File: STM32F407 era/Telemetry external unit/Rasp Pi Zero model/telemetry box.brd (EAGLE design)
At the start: 160 x 100 mm, 14 parts, among them U1 SC18IM700IPW,112

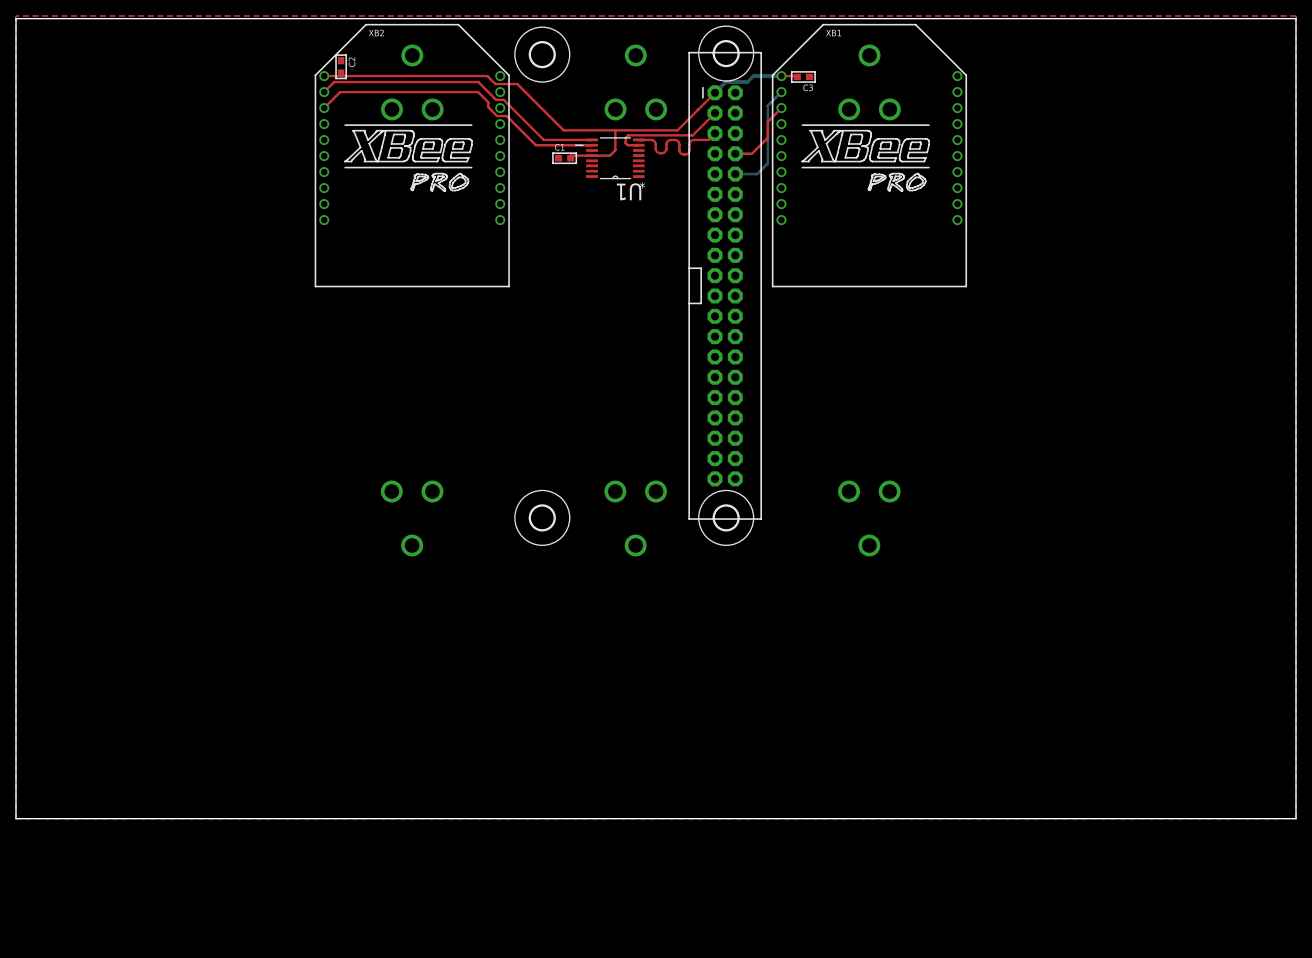
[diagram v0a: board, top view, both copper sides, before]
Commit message: started reworking the board for better charging
started reworking the battery solution to incorporate parallel cell
charging.
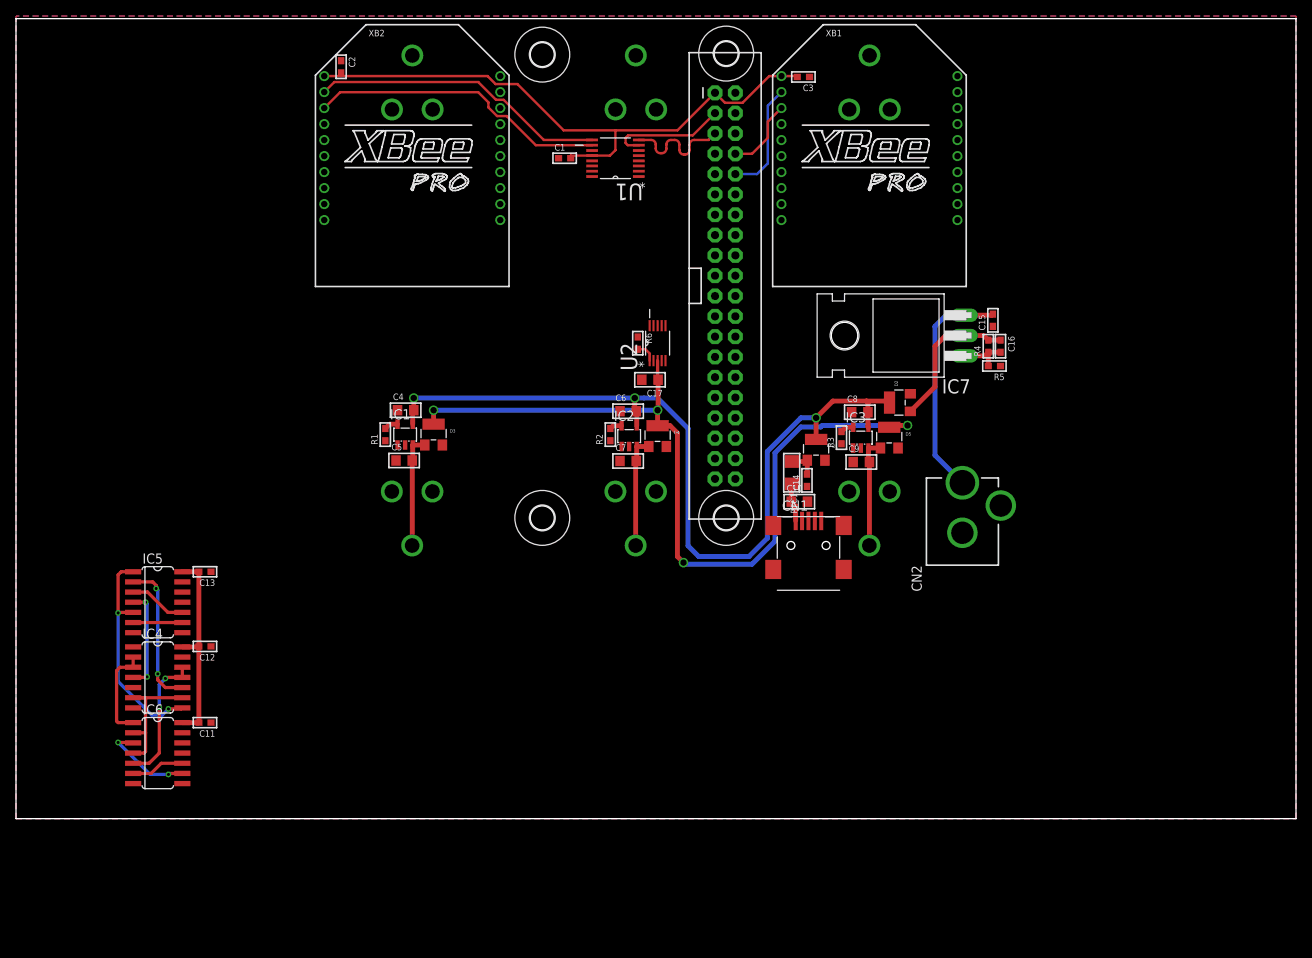
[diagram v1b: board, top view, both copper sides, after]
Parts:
- added C10, C17, C4, C5, C6, C7, C8, C9: 10u, microbuilder:_0805
- added C11, C12, C13, C14, C15: 100n, microbuilder:_0603
- added C16: 1u-T, microbuilder:_0603
- added CN1: (no value), adafruit:USB-MINIB
- added CN2: (no value), adafruit:DCJACK_2MM_PTH
- added D1, D2, D3, D4, D5: (no value), adafruit:SOT23-W
- added IC1, IC2, IC3: MCP73831/OT, adafruit:SOT23-5L
- added IC4: 74AC14D, 74xx-eu:SO14
- added IC5: 74HC08D, 74xx-eu:SO14
- added IC6: 74AC32D, 74xx-eu:SO14
- added IC7: 317T, linear:TO220H
- added PTC1: (no value), microbuilder:1206
- added R1, R2, R3: 5k, microbuilder:_0603
- added R4: 240, microbuilder:_0603
- added R5: 732, microbuilder:_0603
- added R6: 30k1, microbuilder:_0603
- added U2: LTC3402EMSPBF, LTC_By_element14_Batch_1:SOP50P490X110-10N
- turned BAT1 to 90 degrees
- turned BAT2 to 90 degrees
- turned BAT3 to 90 degrees
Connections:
- removed net +: BAT1.PWR@1, BAT2.PWR@1, BAT3.PWR@1
- removed net -: BAT1.GND@1, BAT2.GND@1, BAT3.GND@1
- new net BAT-STAT1: IC1.1, IC4.1
- new net BAT-STAT2: IC2.1, IC4.5
- new net BAT-STAT3: IC3.1, IC4.13
- new net N$1: BAT2.PWR@1, C7.2, D4.1, IC2.3
- new net N$10: IC4.6, IC4.9, IC6.2, IC6.4
- new net N$11: IC4.2, IC4.3, IC6.1
- new net N$12: IC5.6, IC5.9
- new net N$13: IC4.11, IC4.12, IC6.5
- new net N$14: IC4.8, IC5.1, IC5.5
- new net N$15: IC4.10, IC5.2
- new net N$16: IC4.4, IC5.4
- new net N$17: C10.1, CN1.VBUS, PTC1.2
- new net N$18: C16.2, IC7.1, R4.1, R5.2
- new net N$19: R6.2, U2.1
- new net N$2: IC1.5, R1.2
- new net N$20: C16.1, D2.1, IC7.2, R4.2
- new net N$21: C14.2, D1.1, PTC1.1
- new net N$22: C15.2, CN2.PWR, IC7.3
- new net N$3: IC2.5, R2.2
- new net N$4: BAT1.PWR@1, C5.2, D3.1, IC1.3
- new net N$5: IC5.10, IC5.3
- new net N$6: IC6.10, IC6.6
- new net N$7: IC3.5, R3.2
- new net N$8: BAT3.PWR@1, C9.2, D5.1, IC3.3
- new net N$9: IC6.3, IC6.9
- new net VBAT: C17.1, D3.3, D4.3, D5.3, U2.3
- new net VCC: C4.2, C6.2, C8.2, D1.3, D2.3, IC1.4, IC2.4, IC3.4
- net 5.0V: now also C11.2, C12.2, C13.2, IC4.14, IC5.14, IC6.14
- net GND: now also BAT1.GND@1, BAT2.GND@1, BAT3.GND@1, C10.2, C11.1, C12.1, C13.1, C14.1, C15.1, C17.2, C4.1, C5.1, C6.1, C7.1, C8.1, C9.1, CN1.GND, CN2.GND, CN2.GNDBREAK, IC1.2, IC2.2, IC3.2, IC4.7, IC5.12, IC5.13, IC5.7, IC6.12, IC6.13, IC6.7, R1.1, R2.1, R3.1, R5.1, R6.1, U2.2, U2.5
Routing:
- net VCC: track 0.00 -> 103.7 mm, vias 0 -> 3
- net VBAT: track 0.00 -> 101.4 mm, vias 0 -> 4
- net N$22: track 0.00 -> 28.8 mm
- net N$14: track 0.00 -> 27.4 mm, vias 0 -> 2
- net 5.0V: track 0.00 -> 25.1 mm
- net N$15: track 0.00 -> 18.4 mm, vias 0 -> 2
- net N$20: track 0.00 -> 18.4 mm
- net N$10: track 0.00 -> 17.6 mm
- net N$13: track 0.00 -> 16.9 mm, vias 0 -> 2
- net N$4: track 0.00 -> 14.1 mm
- net N$1: track 0.00 -> 13.9 mm
- net N$8: track 0.00 -> 13.7 mm
- net N$16: track 0.00 -> 12.7 mm, vias 0 -> 2
- net N$11: track 0.00 -> 12.0 mm
- net N$9: track 0.00 -> 11.6 mm, vias 0 -> 2
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
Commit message: minor changes to layout
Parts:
- added C18, C19: 1u, microbuilder:_0603
- added R7, R8: 850, microbuilder:_0603
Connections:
- new net LAPRSSISENSE: C19.2, R8.2
- new net N$23: R7.1, XB1.6
- new net N$24: R8.1, XB2.6
- new net TELERSSISENSE: C18.2, R7.2
- net 3.3V: now also XB1.5, XB2.5
- net GND: now also C18.1, C19.1
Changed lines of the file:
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@@
 <element name="C17" library="microbuilder" package="_0805" value="10u" x="79.248" y="54.864" rot="R180"/>
 <element name="R6" library="microbuilder" package="_0603" value="30k1" x="77.724" y="59.436" rot="R270"/>
+<element name="R7" library="microbuilder" package="_0603" value="850" x="1.6891" y="-2.26695"/>
+<element name="C18" library="microbuilder" package="_0603" value="1u" x="1.6891" y="-6.4008"/>
+<element name="R8" library="microbuilder" package="_0603" value="850" x="1.6891" y="-10.53465"/>
+<element name="C19" library="microbuilder" package="_0603" value="1u" x="1.6891" y="-14.6685"/>
 </elements>
 <signals>
@@
 <wire x1="72.009" y1="82.8802" x2="69.342" y2="82.8802" width="0.3048" layer="1"/>
 <wire x1="69.342" y1="82.8802" x2="69.342" y2="82.55" width="0.3048" layer="1"/>
-<wire x1="62.6745" y1="91.821" x2="68.453" y2="86.0425" width="0.3048" layer="1"/>
+<wire x1="61.29655" y1="91.821" x2="67.07505" y2="86.0425" width="0.3048" layer="1"/>
 <wire x1="72.009" y1="82.8802" x2="74.2442" y2="82.8802" width="0.3048" layer="1"/>
 <wire x1="74.2442" y1="82.8802" x2="74.93" y2="83.566" width="0.3048" layer="1"/>
 <wire x1="74.93" y1="83.566" x2="74.93" y2="86.0425" width="0.3048" layer="1"/>
-<wire x1="62.6745" y1="91.821" x2="59.944" y2="91.821" width="0.3048" layer="1"/>
+<wire x1="61.29655" y1="91.821" x2="59.944" y2="91.821" width="0.3048" layer="1"/>
 <wire x1="59.944" y1="91.821" x2="58.945" y2="92.82" width="0.3048" layer="1"/>
 <wire x1="58.945" y1="92.82" x2="40.64" y2="92.82" width="0.3048" layer="1"/>
 <wire x1="40.64" y1="92.82" x2="38.53" y2="92.82" width="0.3048" layer="1"/>
 <wire x1="40.64" y1="93.218" x2="40.64" y2="92.82" width="0.3048" layer="1"/>
-<wire x1="68.453" y1="86.0425" x2="74.93" y2="86.0425" width="0.3048" layer="1"/>
+<wire x1="67.07505" y1="86.0425" x2="74.93" y2="86.0425" width="0.3048" layer="1"/>
 <wire x1="74.93" y1="86.0425" x2="82.6897" y2="86.0425" width="0.3048" layer="1"/>
 <wire x1="82.6897" y1="86.0425" x2="87.376" y2="90.7288" width="0.3048" layer="1"/>
@@
 <wire x1="90.81135" y1="89.47785" x2="94.1535" y2="92.82" width="0.3048" layer="1"/>
 <wire x1="94.1535" y1="92.82" x2="95.68" y2="92.82" width="0.3048" layer="1"/>
-<wire x1="82.6897" y1="86.0425" x2="87.376" y2="70.4088" width="0" layer="19" extent="1-1"/>
+<contactref element="XB1" pad="5"/>
+<contactref element="XB2" pad="5"/>
+<wire x1="90.81135" y1="89.47785" x2="95.68" y2="84.82" width="0" layer="19" extent="1-1"/>
+<wire x1="38.53" y1="84.82" x2="38.53" y2="92.82" width="0" layer="19" extent="1-1"/>
+<wire x1="87.376" y1="70.4088" x2="82.6897" y2="86.0425" width="0" layer="19" extent="1-1"/>
 </signal>
 <signal name="GND">
@@
 <contactref element="U2" pad="2"/>
 <contactref element="R6" pad="1"/>
+<contactref element="C18" pad="1"/>
+<contactref element="C19" pad="1"/>
+<wire x1="0.9271" y1="-6.4008" x2="0.9271" y2="-14.6685" width="0" layer="19" extent="1-1"/>
+<wire x1="14.6431" y1="4.3815" x2="0.9271" y2="-6.4008" width="0" layer="19" extent="1-1"/>
 </signal>
 <signal name="5.0V">
@@
 <wire x1="78.6765" y1="58.674" x2="77.724" y2="58.674" width="0.3048" layer="1"/>
 </signal>
+<signal name="N$23">
+<contactref element="XB1" pad="6"/>
+<contactref element="R7" pad="1"/>
+<wire x1="0.9271" y1="-2.26695" x2="95.68" y2="82.82" width="0" layer="19" extent="1-1"/>
+</signal>
+<signal name="TELERSSISENSE">
+<contactref element="R7" pad="2"/>
+<contactref element="C18" pad="2"/>
+<wire x1="2.4511" y1="-2.26695" x2="2.4511" y2="-6.4008" width="0" layer="19" extent="1-1"/>
+</signal>
+<signal name="N$24">
+<contactref element="XB2" pad="6"/>
+<contactref element="R8" pad="1"/>
+<wire x1="0.9271" y1="-10.53465" x2="38.53" y2="82.82" width="0" layer="19" extent="1-1"/>
+</signal>
+<signal name="LAPRSSISENSE">
+<contactref element="R8" pad="2"/>
+<contactref element="C19" pad="2"/>
+<wire x1="2.4511" y1="-10.53465" x2="2.4511" y2="-14.6685" width="0" layer="19" extent="1-1"/>
+</signal>
 </signals>

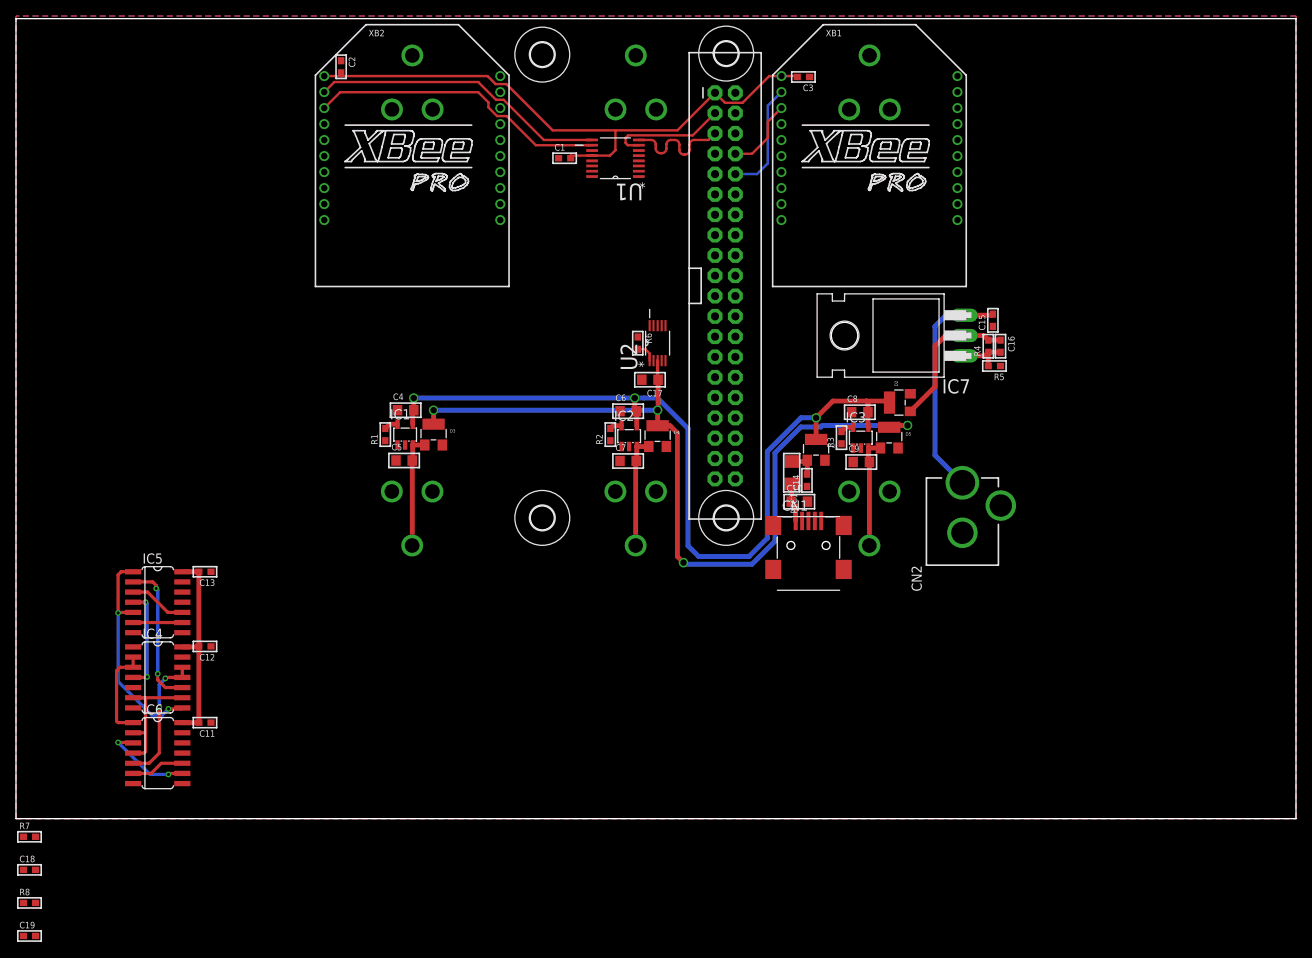
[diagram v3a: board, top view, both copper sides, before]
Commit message: started working on the power circuitry
started work on 5V boost circuit for the battery powered operation
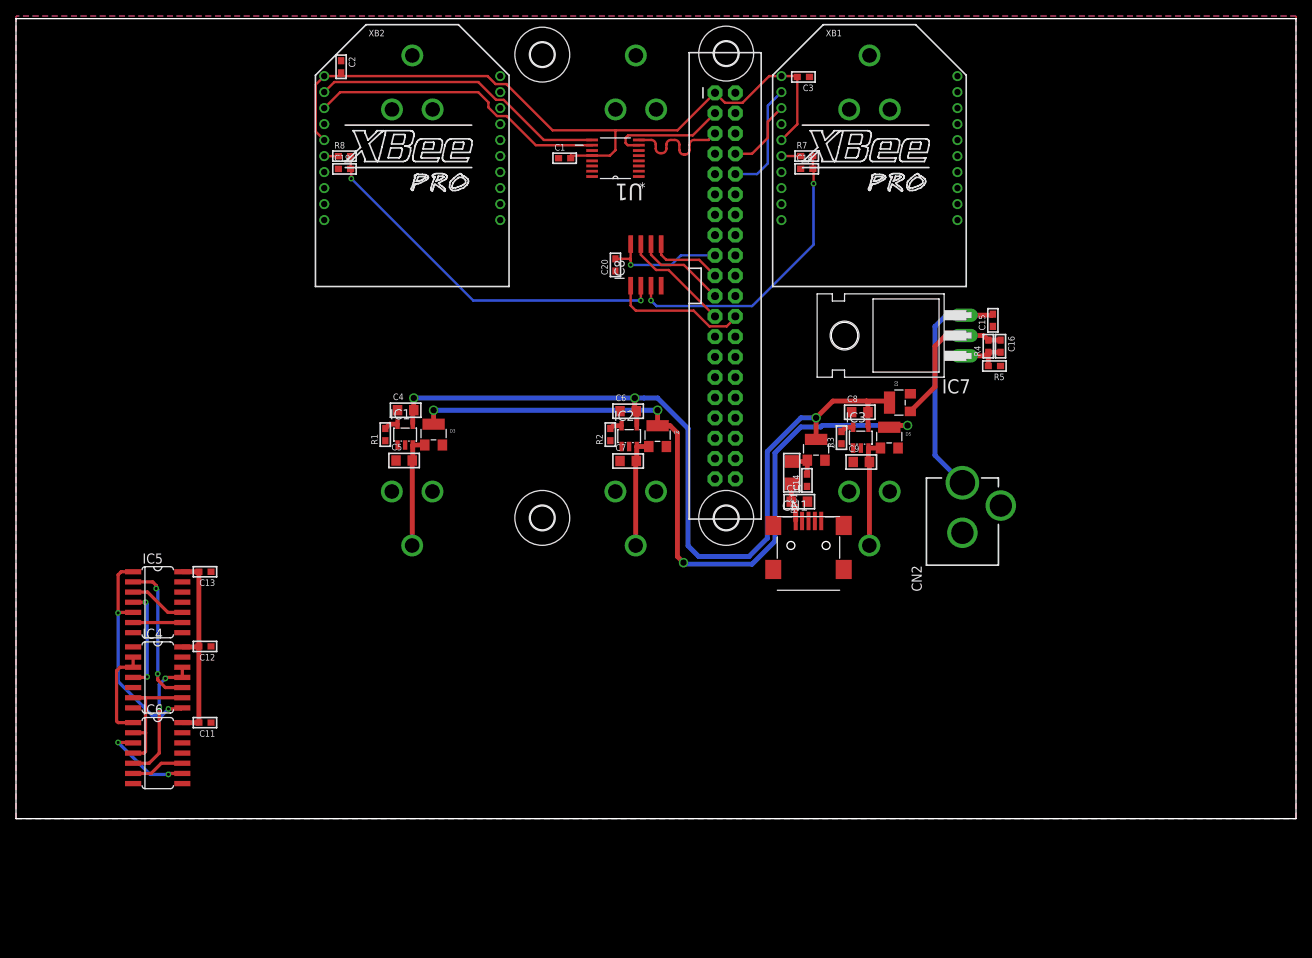
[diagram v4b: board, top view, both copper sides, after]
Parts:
- removed C17: 10u, microbuilder:_0805
- removed R6: 30k1, microbuilder:_0603
- removed U2: LTC3402EMSPBF, LTC_By_element14_Batch_1:SOP50P490X110-10N
- added C20: 100n, microbuilder:_0603
- added IC8: MCP3202SN, microchip:SO-08
- moved C18 130.8 mm to (98.8, 81.2)
- moved R7 129.1 mm to (98.8, 82.8)
- moved C19 103.7 mm to (41.1, 81.2)
- moved R8 101.3 mm to (41.1, 82.8)
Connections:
- removed net N$19: R6.2, U2.1
- new net CE0: IC8.1, JP1.24
- new net MISO: IC8.6, JP1.21
- new net MOSI: IC8.5, JP1.19
- new net SCLK: IC8.7, JP1.23
- net 3.3V: now also C11.2, C12.2, C13.2, C20.2, IC4.14, IC5.14, IC6.14, IC8.8
- net 5.0V: no longer C11.2, C12.2, C13.2, IC4.14, IC5.14, IC6.14
- net GND: now also C20.1, IC8.4; no longer C17.2, R6.1, U2.2, U2.5
- net LAPRSSISENSE: now also IC8.2
- net TELERSSISENSE: now also IC8.3
- net VBAT: no longer C17.1, U2.3
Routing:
- net 3.3V: track 74.9 -> 133.2 mm, vias 0 -> 1
- net LAPRSSISENSE: track 0.00 -> 47.2 mm, vias 0 -> 2
- net TELERSSISENSE: track 0.00 -> 36.8 mm, vias 0 -> 2
- net 5.0V: track 25.1 -> 0.00 mm
- net CE0: track 0.00 -> 17.3 mm
- net SCLK: track 0.00 -> 13.8 mm
- net MISO: track 0.00 -> 11.5 mm
- net MOSI: track 0.00 -> 9.14 mm
- net VBAT: track 101.4 -> 95.3 mm
- net N$19: track 2.60 -> 0.00 mm
- net N$23: track 0.00 -> 2.40 mm
- net N$24: track 0.00 -> 1.78 mm
